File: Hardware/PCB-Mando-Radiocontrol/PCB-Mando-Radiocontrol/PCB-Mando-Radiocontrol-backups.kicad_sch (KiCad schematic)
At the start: 25 parts, among them J1 nombre del prog, U1 ATMEGA328P, U2 Nrf24l01, U3 AMS1117-3.3, U4 AMS1117-5.0, U5 COM-09032, U6 COM-09032, Y1 16MHZ

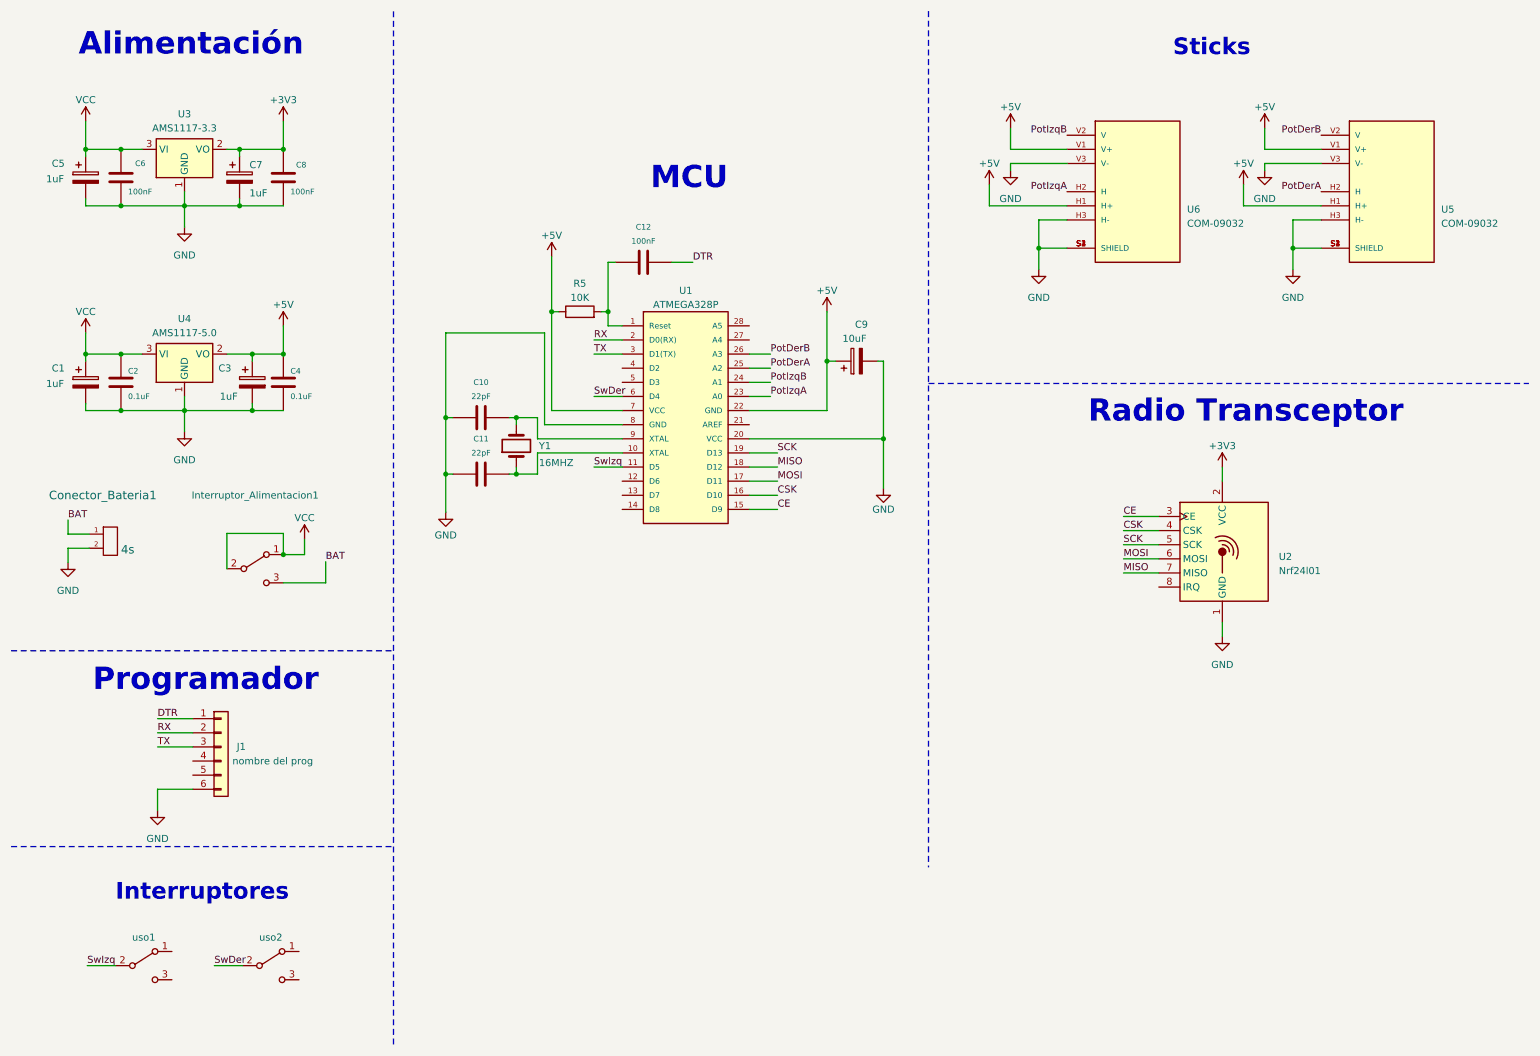
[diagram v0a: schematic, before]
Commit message: Cambios en el kicad_sch realice cambios del programador y del capacitor de filtro para el uC ademas rellene el rotulo
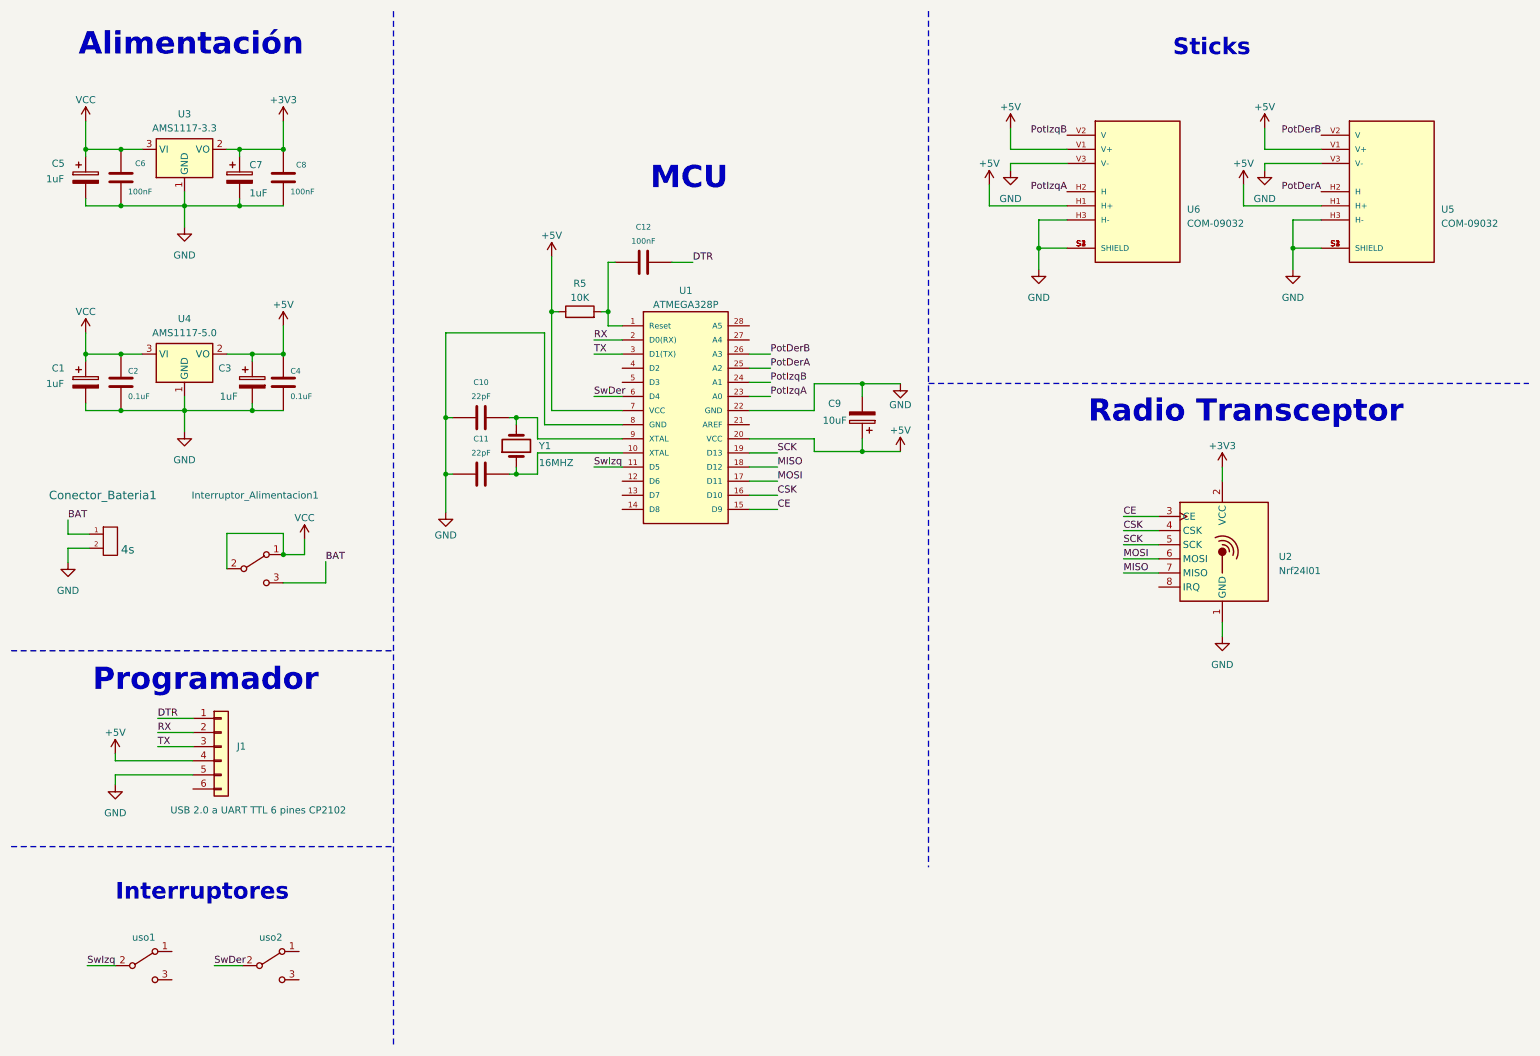
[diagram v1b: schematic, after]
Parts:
- J1: value nombre del prog -> USB 2.0 a UART TTL 6 pines CP2102
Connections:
- net +5V: now also J1.4 (Pin_4), U1.20 (VCC); no longer U1.22 (GND)
- net GND: now also J1.5 (Pin_5), U1.22 (GND); no longer J1.6 (Pin_6), U1.20 (VCC)
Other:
- company: (none) -> E.E.S.T.Nº5 "2 DE ABRIL" TEMPERLEY
- title: (none) -> Mando-Radiocontrol-Dron
- moved on the sheet: C9
